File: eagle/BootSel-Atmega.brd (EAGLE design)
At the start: 58.7 x 22.2 mm, 9 parts, among them Q1 20MHz

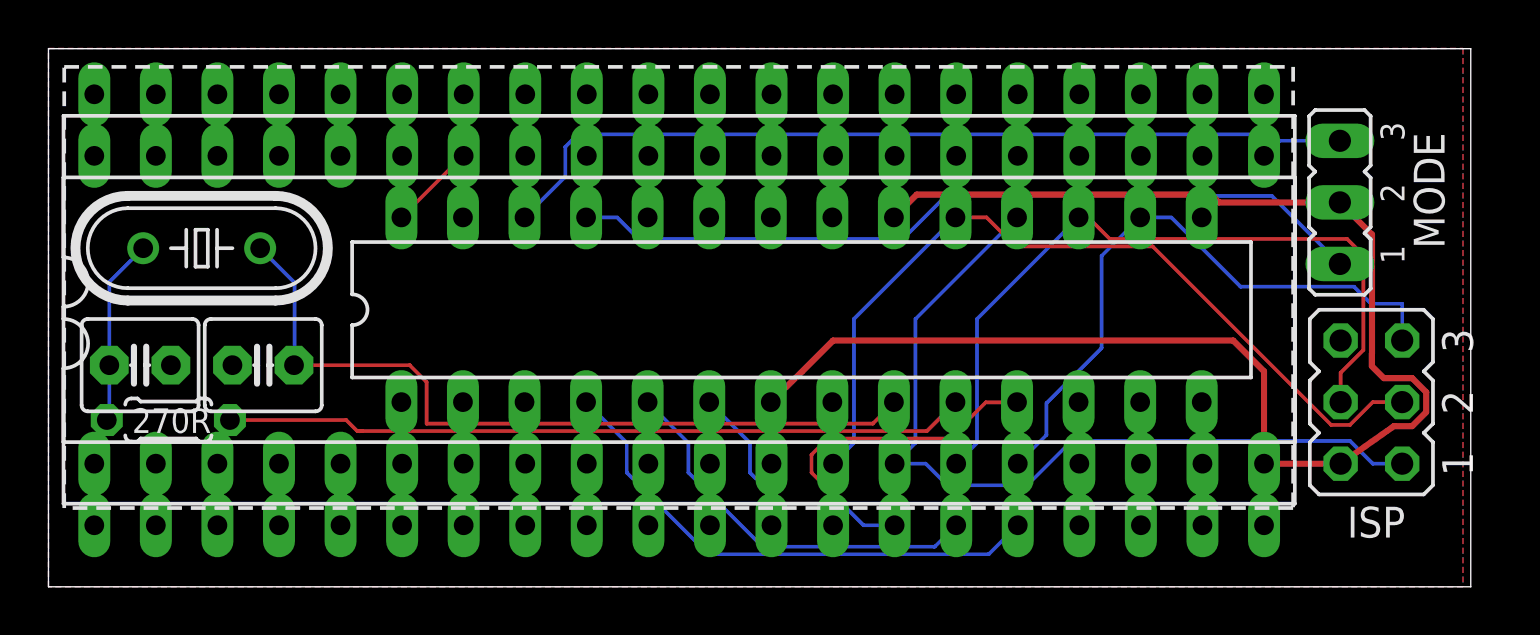
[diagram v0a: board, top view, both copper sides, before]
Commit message: Fixed ISP connecotor.
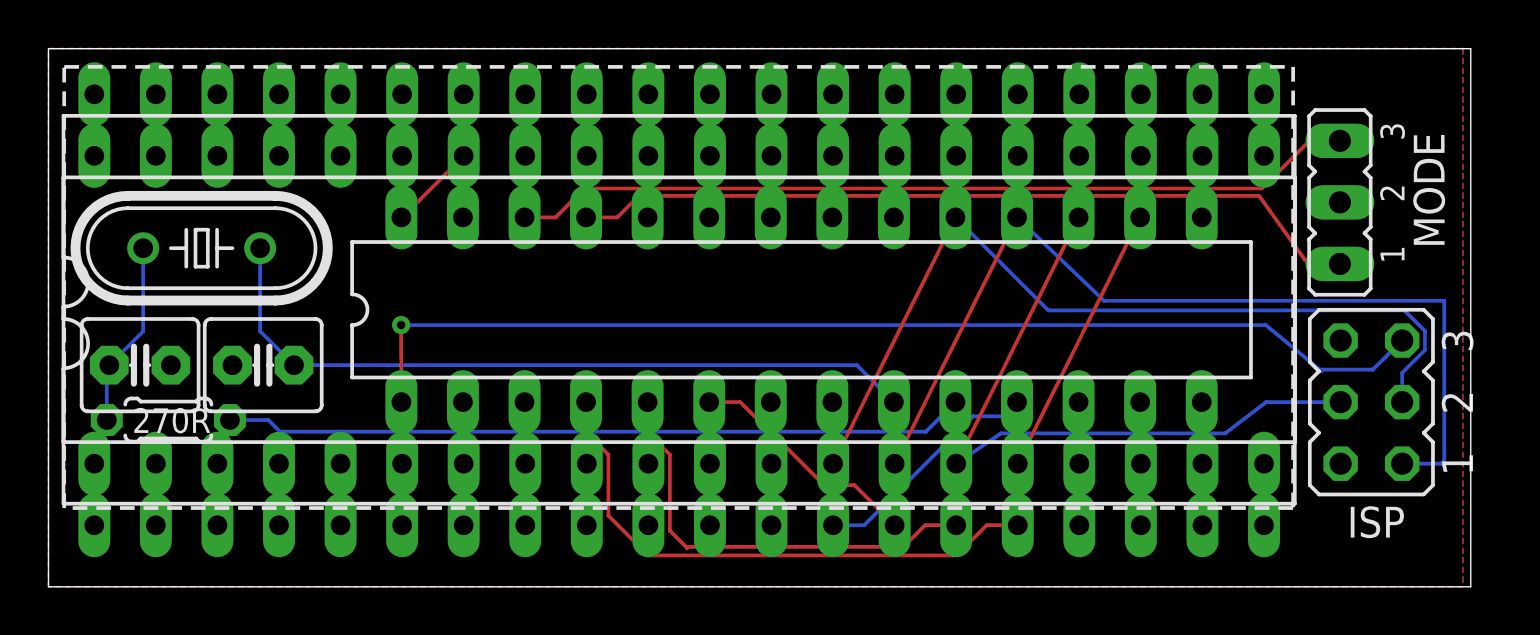
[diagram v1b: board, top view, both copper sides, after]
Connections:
- removed net ISP_RST: BOARD.16, ISP.5, MEGA.16
- new net /ISP_RST: ISP.5, MEGA.1
- new net /SEL3: BOARD.16, MEGA.16
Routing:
- net VCC: track 65.4 -> 0.00 mm
- net /ISP_RST: track 0.00 -> 45.7 mm, vias 0 -> 1
- net ISP_RST: track 26.1 -> 0.00 mm
- net /SEL3: track 0.00 -> 11.3 mm
- net MISO: track 34.7 -> 38.7 mm
- net MOSI: track 31.1 -> 28.0 mm
- net /NEWSEL0: track 12.7 -> 9.69 mm
- net N$17: track 32.8 -> 30.8 mm
- net /NEWSEL2: track 16.3 -> 18.2 mm
- net /NEWSEL3: track 21.6 -> 23.2 mm
- net SCK: track 34.6 -> 36.0 mm
- net MODE2: track 35.9 -> 34.9 mm
- net /NEWSEL1: track 10.5 -> 9.75 mm
- added copper zone on layer 1, net VCC
- removed copper zone on layer 1, net GND
